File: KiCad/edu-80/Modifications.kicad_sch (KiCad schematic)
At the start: 4 parts, among them U101 7408, U102 74LS190, U103 74LS74, X1 20MHz Ocillator

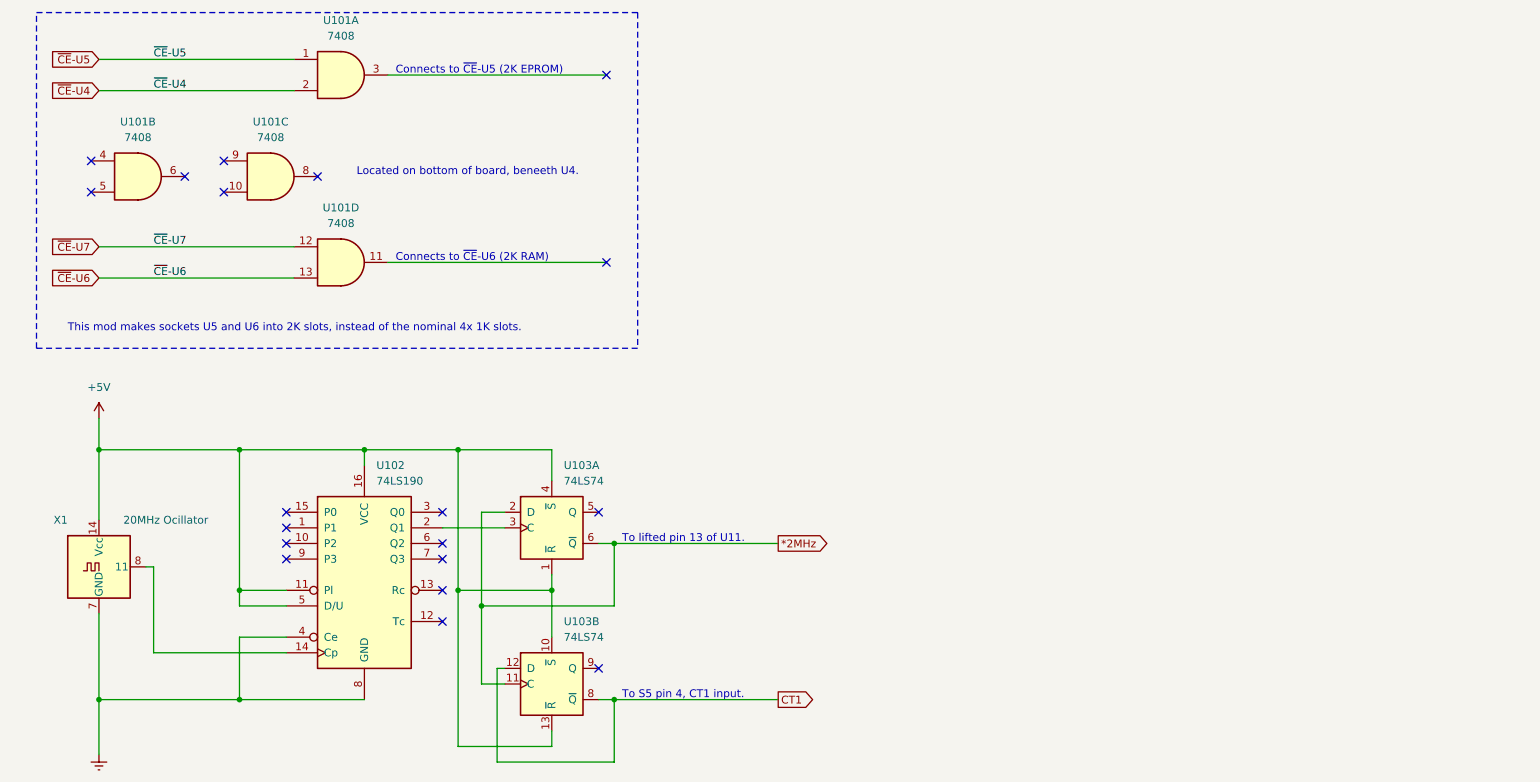
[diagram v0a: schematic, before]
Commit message: Fixed ~IRQ vs. INT for PIO/CTC. Removed old (version 5) schematic files.
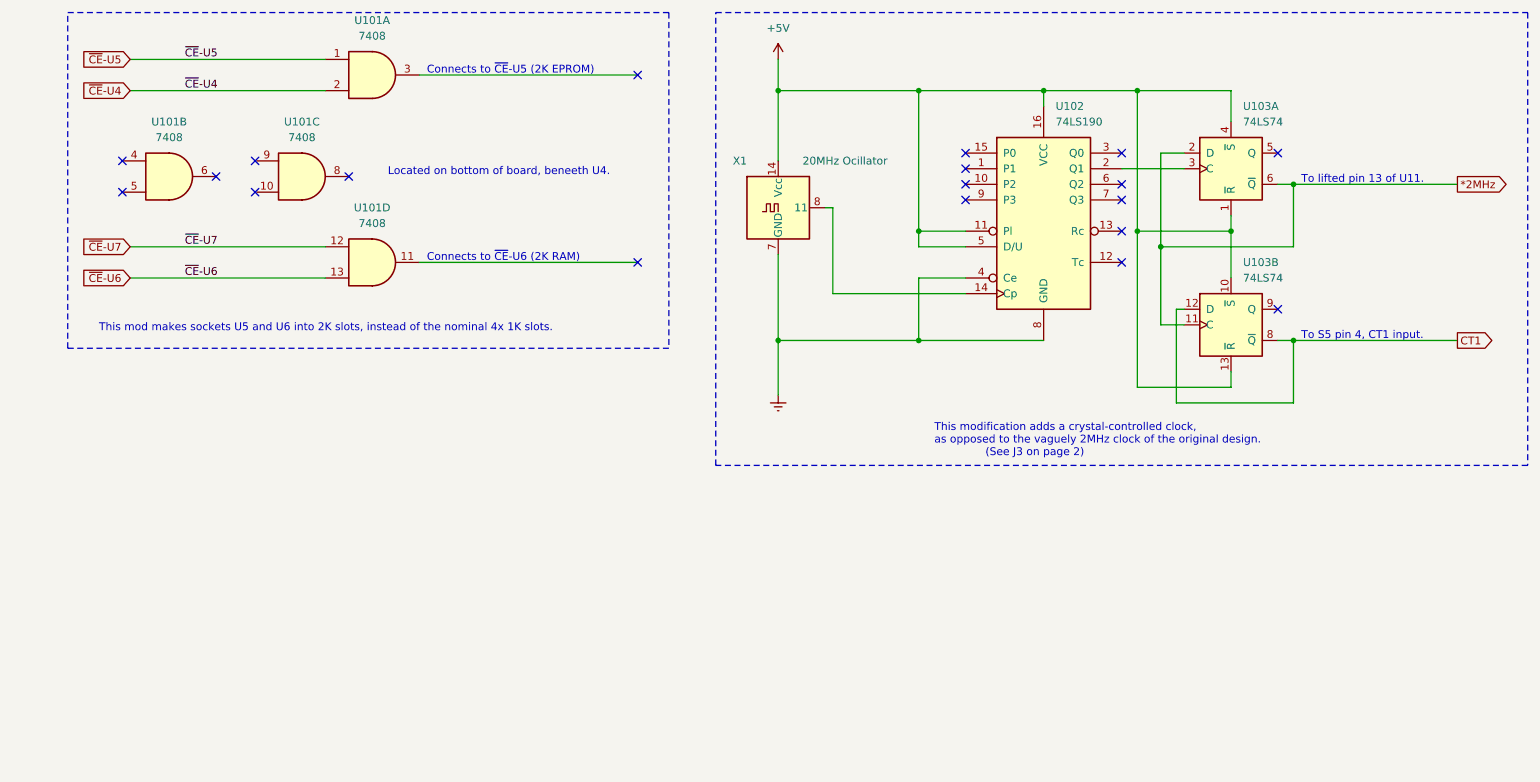
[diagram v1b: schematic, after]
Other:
- note added: "This modification adds a crystal-controlled clock, as opposed to the vaguely 2MHz clock of the original design. (See J3 on page 2)"
- moved on the sheet: U101A, U101B, U101C, U101D, U102, U103A, U103B, X1

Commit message: Fixed the last of the EDR warnings/errors, adding footprints
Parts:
- U101: footprint (none) -> Package_DIP:DIP-14_W7.62mm
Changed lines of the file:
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@@
       (effects (font (size 1.27 1.27)))
     )
-    (property "Footprint" "" (at 69.85 24.13 0)
+    (property "Footprint" "Package_DIP:DIP-14_W7.62mm" (at 69.85 24.13 0)
       (effects (font (size 1.27 1.27)) hide)
     )
@@
       (effects (font (size 1.27 1.27)))
     )
-    (property "Footprint" "" (at 69.85 54.61 0)
+    (property "Footprint" "Package_DIP:DIP-14_W7.62mm" (at 69.85 54.61 0)
       (effects (font (size 1.27 1.27)) hide)
     )
@@
       (effects (font (size 1.27 1.27)))
     )
-    (property "Footprint" "" (at 36.83 40.64 0)
+    (property "Footprint" "Package_DIP:DIP-14_W7.62mm" (at 36.83 40.64 0)
       (effects (font (size 1.27 1.27)) hide)
     )
@@
       (effects (font (size 1.27 1.27)))
     )
-    (property "Footprint" "" (at 58.42 40.64 0)
+    (property "Footprint" "Package_DIP:DIP-14_W7.62mm" (at 58.42 40.64 0)
       (effects (font (size 1.27 1.27)) hide)
     )
